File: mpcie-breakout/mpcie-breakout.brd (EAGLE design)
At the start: 50 x 70 mm, 34 parts, among them K1 694108106102, U1 IP4234CZ6, U2 LD1085D2T33R, X1 MPCIE-JAE, X2 MINI-USB-SHIELD-UX60-MB-5ST

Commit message: mpci-breakout: Add BOM attributes + export BOM
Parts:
- R1, R2, R3: value (none) -> 47

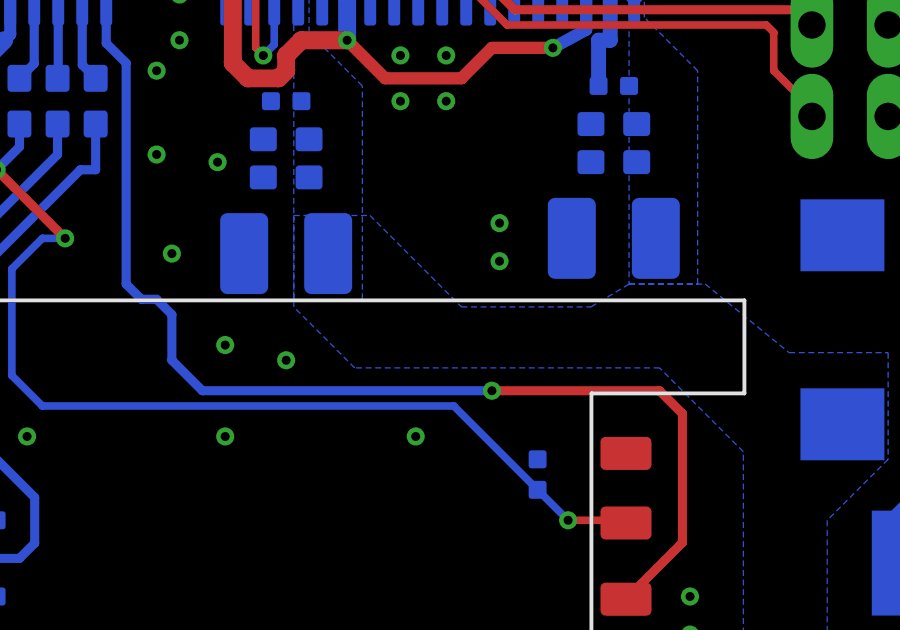
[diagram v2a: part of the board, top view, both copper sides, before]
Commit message: mpcie-breakout: change 100uF caps from 1210 to 1206, reducing height
The current 100uF caps are too high at 2.9mm.  They touch the shielding
can of Quectel EC-20 modules, for exampel.  Let's use 1206 packaged
versions at 1.6mm instead.  Also, add two more, for safety.
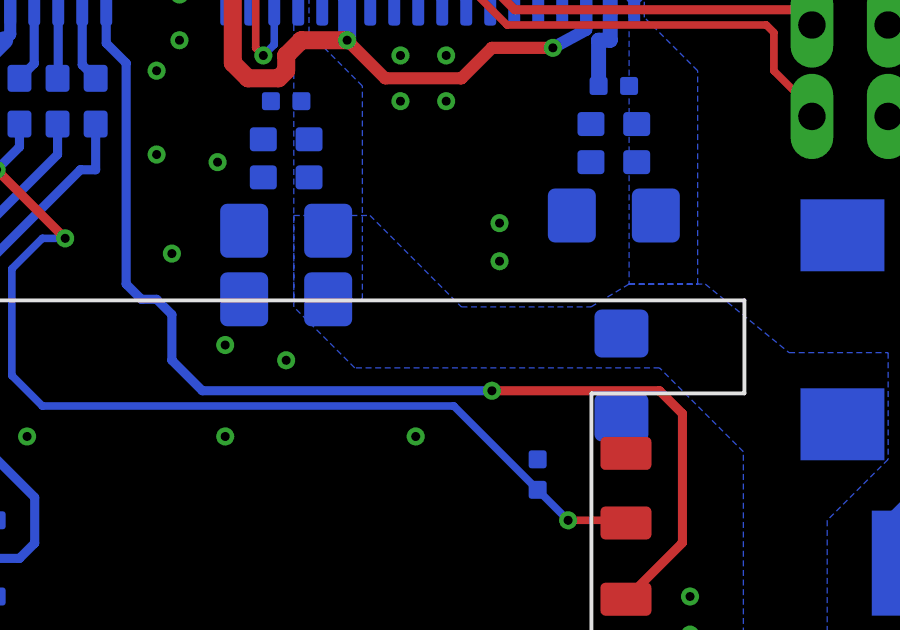
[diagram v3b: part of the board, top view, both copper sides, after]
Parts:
- added C10, C11: 100u, rc-sysmocom:1206
- C105, C109: device rc-sysmocom:C1210 -> rc-sysmocom:1206
- moved C105 0.76 mm to (16.5, 42.7)
- moved C109 0.76 mm to (27.4, 43.2)
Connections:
- net GND: now also C10.1, C11.1
- net VCC_3V3: now also C10.2, C11.2

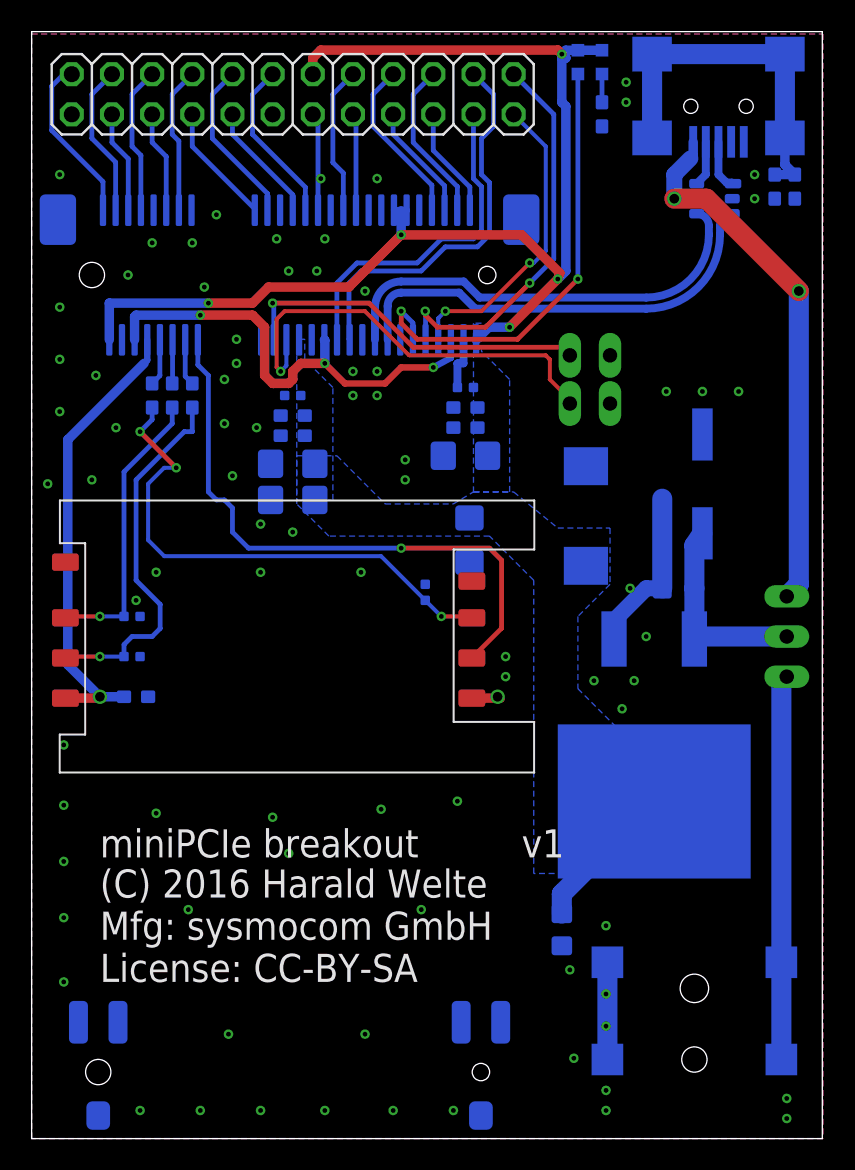
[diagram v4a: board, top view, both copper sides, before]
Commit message: mpcie-breakout: Add series LED for LED_WWAN
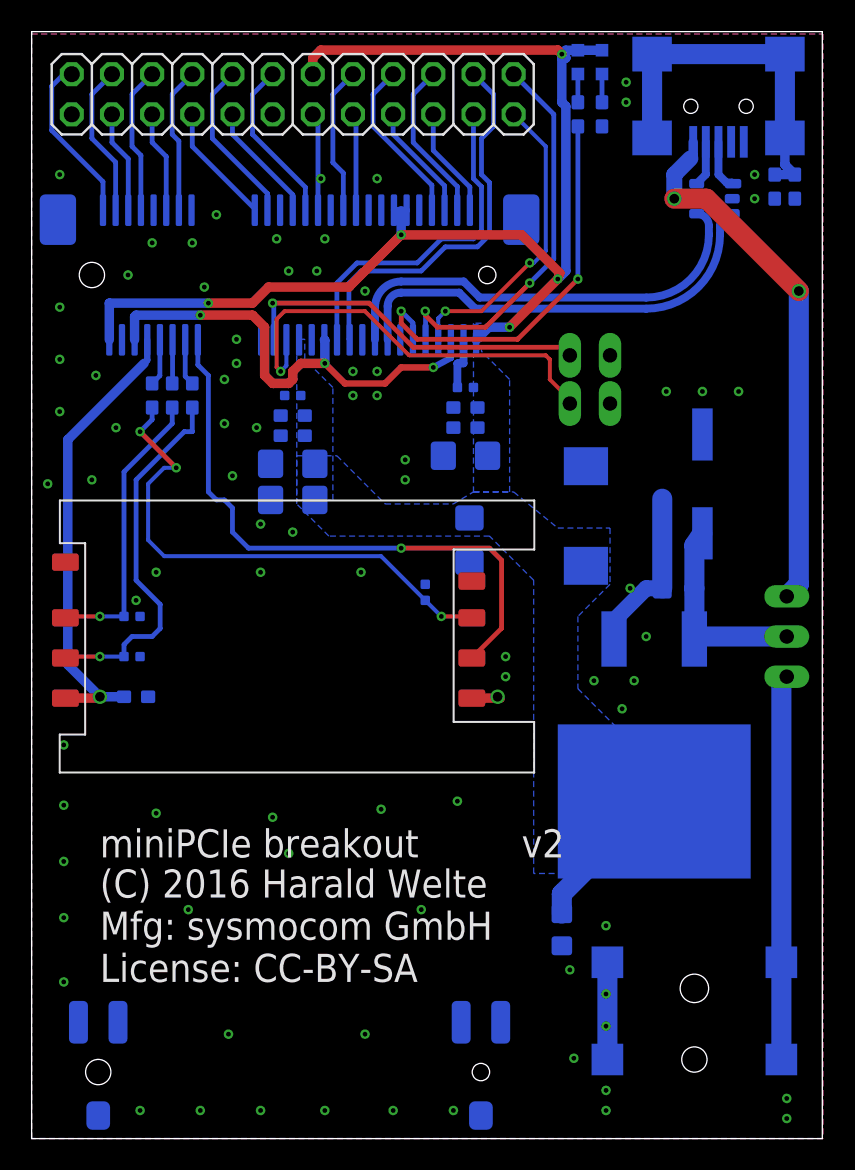
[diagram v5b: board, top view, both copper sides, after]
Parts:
- added R6: 330, rc-sysmocom:_0603
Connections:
- new net N$2: LED1.C, R6.1
- net N$3: now also R6.2; no longer LED1.C
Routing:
- net N$3: track 29.0 -> 25.7 mm
- net N$2: track 0.00 -> 1.79 mm
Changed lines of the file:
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@@
 </plain>
 <attributes>
-<attribute name="VERSION" value="v1"/>
+<attribute name="VERSION" value="v2"/>
 </attributes>
 <variantdefs>
@@
 <attribute name="VALUE" x="25.781" y="36.2585" size="0.508" layer="28" font="vector" ratio="10" rot="MR90"/>
 </element>
+<element name="R6" library="rc-sysmocom" package="_0603" value="330" x="34.544" y="64.77" rot="MR270">
+<attribute name="LINK" value="http://www.digikey.com/product-detail/en/yageo/RC0603JR-07330RL/311-330GRCT-ND/729716" x="34.544" y="64.77" size="1.778" layer="28" rot="MR270" display="off"/>
+<attribute name="MANUFACTURERPARTNUMBER" value="RC0603JR-07330RL" x="34.544" y="64.77" size="1.778" layer="28" rot="MR270" display="off"/>
+<attribute name="ROHSCERTIFICATE" value="UNKNOWN ROHS CERTIFICATE" x="34.544" y="64.77" size="1.778" layer="28" rot="MR270" display="off"/>
+<attribute name="SOURCE" value="DIGIKEY" x="34.544" y="64.77" size="1.778" layer="28" rot="MR270" display="off"/>
+<attribute name="CLASS" value="RESISTOR" x="34.544" y="64.77" size="1.778" layer="28" rot="MR270" display="off"/>
+<attribute name="POPULATED" value="TRUE" x="34.544" y="64.77" size="1.778" layer="28" rot="MR270" display="off"/>
+<attribute name="MANUFACTURER" value="Yageo" x="34.544" y="64.77" size="1.778" layer="28" rot="MR270" display="off"/>
+<attribute name="SOURCEPARTNUMBER" value="311-330GRCT-ND" x="34.544" y="64.77" size="1.778" layer="28" rot="MR270" display="off"/>
+<attribute name="DESCRIPTION" value="RES SMD 330 OHM 5% 1/10W 0603" x="34.544" y="64.77" size="1.778" layer="28" rot="MR270" display="off"/>
+</element>
 </elements>
 <signals>
@@
 <signal name="N$3">
 <contactref element="X1" pad="42"/>
-<contactref element="LED1" pad="C"/>
 <wire x1="24.111875" y1="50.51" x2="24.111875" y2="51.580125" width="0.3048" layer="16"/>
 <wire x1="24.111875" y1="51.580125" x2="23.368" y2="52.324" width="0.3048" layer="16"/>
@@
 <wire x1="30.734" y1="50.546" x2="34.544" y2="54.356" width="0.3048" layer="1"/>
 <via x="34.544" y="54.356" extent="1-16" drill="0.3"/>
-<wire x1="34.544" y1="54.356" x2="34.544" y2="67.322" width="0.3048" layer="16"/>
+<contactref element="R6" pad="2"/>
+<wire x1="34.544" y1="54.356" x2="34.544" y2="64.008" width="0.3048" layer="16"/>
 </signal>
 <signal name="N$4">
@@
 <wire x1="36.068" y1="67.322" x2="36.068" y2="65.532" width="0.3048" layer="16"/>
 </signal>
+<signal name="N$2">
+<contactref element="LED1" pad="C"/>
+<contactref element="R6" pad="1"/>
+<wire x1="34.544" y1="67.322" x2="34.544" y2="65.532" width="0.3048" layer="16"/>
+</signal>
 </signals>

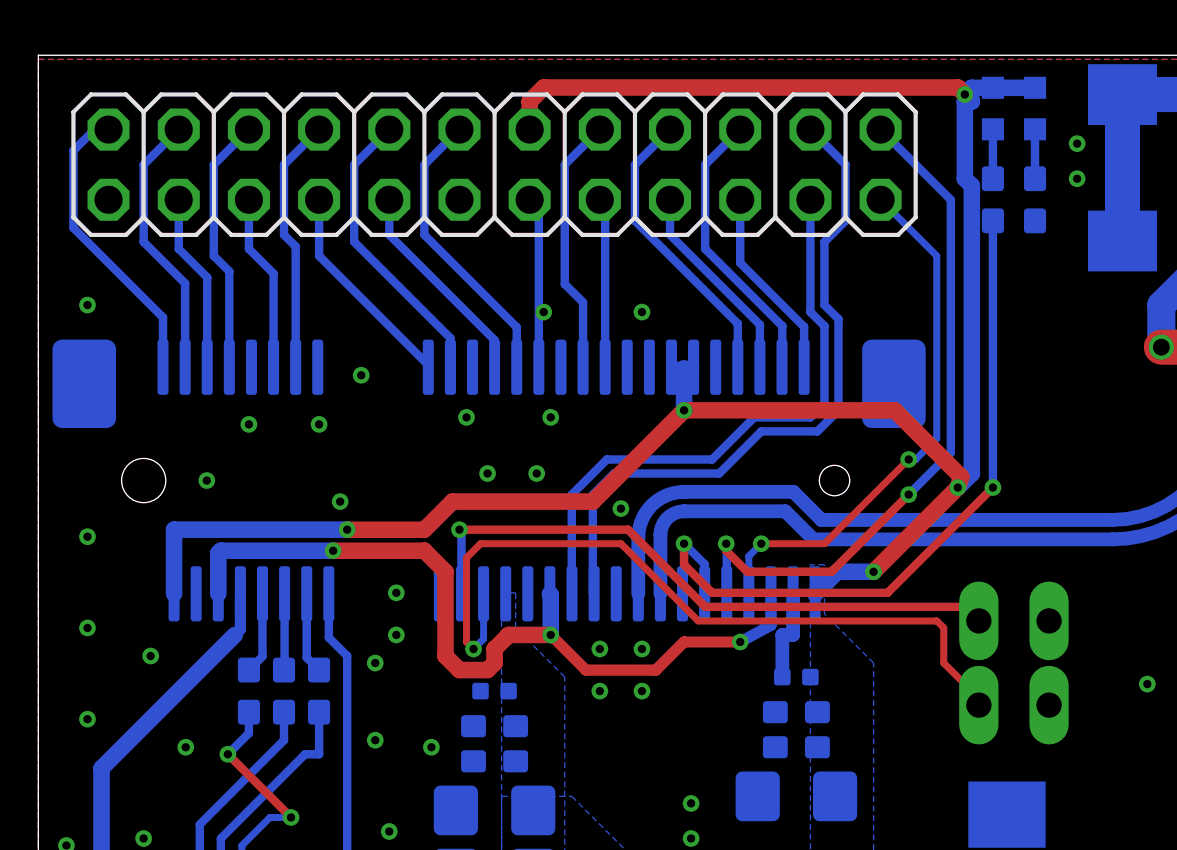
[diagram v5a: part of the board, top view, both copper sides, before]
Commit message: mpcie-breakout: fix DRC violations (clearance)
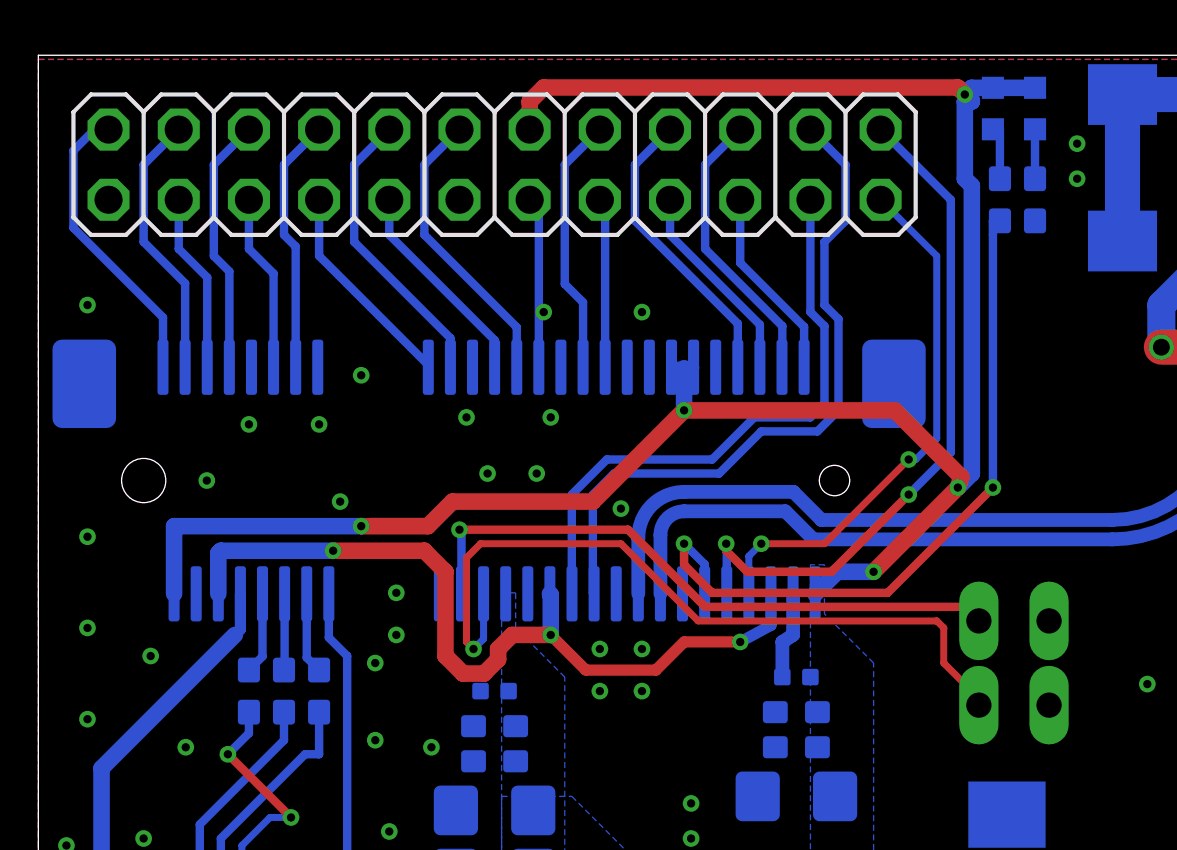
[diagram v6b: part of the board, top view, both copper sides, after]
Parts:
- moved R6 0.25 mm to (34.8, 64.8)
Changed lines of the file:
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@@
 <attribute name="VALUE" x="25.781" y="36.2585" size="0.508" layer="28" font="vector" ratio="10" rot="MR90"/>
 </element>
-<element name="R6" library="rc-sysmocom" package="_0603" value="330" x="34.544" y="64.77" rot="MR270">
-<attribute name="LINK" value="http://www.digikey.com/product-detail/en/yageo/RC0603JR-07330RL/311-330GRCT-ND/729716" x="34.544" y="64.77" size="1.778" layer="28" rot="MR270" display="off"/>
-<attribute name="MANUFACTURERPARTNUMBER" value="RC0603JR-07330RL" x="34.544" y="64.77" size="1.778" layer="28" rot="MR270" display="off"/>
-<attribute name="ROHSCERTIFICATE" value="UNKNOWN ROHS CERTIFICATE" x="34.544" y="64.77" size="1.778" layer="28" rot="MR270" display="off"/>
-<attribute name="SOURCE" value="DIGIKEY" x="34.544" y="64.77" size="1.778" layer="28" rot="MR270" display="off"/>
-<attribute name="CLASS" value="RESISTOR" x="34.544" y="64.77" size="1.778" layer="28" rot="MR270" display="off"/>
-<attribute name="POPULATED" value="TRUE" x="34.544" y="64.77" size="1.778" layer="28" rot="MR270" display="off"/>
-<attribute name="MANUFACTURER" value="Yageo" x="34.544" y="64.77" size="1.778" layer="28" rot="MR270" display="off"/>
-<attribute name="SOURCEPARTNUMBER" value="311-330GRCT-ND" x="34.544" y="64.77" size="1.778" layer="28" rot="MR270" display="off"/>
-<attribute name="DESCRIPTION" value="RES SMD 330 OHM 5% 1/10W 0603" x="34.544" y="64.77" size="1.778" layer="28" rot="MR270" display="off"/>
+<element name="R6" library="rc-sysmocom" package="_0603" value="330" x="34.798" y="64.77" rot="MR270">
+<attribute name="LINK" value="http://www.digikey.com/product-detail/en/yageo/RC0603JR-07330RL/311-330GRCT-ND/729716" x="34.798" y="64.77" size="1.778" layer="28" rot="MR270" display="off"/>
+<attribute name="MANUFACTURERPARTNUMBER" value="RC0603JR-07330RL" x="34.798" y="64.77" size="1.778" layer="28" rot="MR270" display="off"/>
+<attribute name="ROHSCERTIFICATE" value="UNKNOWN ROHS CERTIFICATE" x="34.798" y="64.77" size="1.778" layer="28" rot="MR270" display="off"/>
+<attribute name="SOURCE" value="DIGIKEY" x="34.798" y="64.77" size="1.778" layer="28" rot="MR270" display="off"/>
+<attribute name="CLASS" value="RESISTOR" x="34.798" y="64.77" size="1.778" layer="28" rot="MR270" display="off"/>
+<attribute name="POPULATED" value="TRUE" x="34.798" y="64.77" size="1.778" layer="28" rot="MR270" display="off"/>
+<attribute name="MANUFACTURER" value="Yageo" x="34.798" y="64.77" size="1.778" layer="28" rot="MR270" display="off"/>
+<attribute name="SOURCEPARTNUMBER" value="311-330GRCT-ND" x="34.798" y="64.77" size="1.778" layer="28" rot="MR270" display="off"/>
+<attribute name="DESCRIPTION" value="RES SMD 330 OHM 5% 1/10W 0603" x="34.798" y="64.77" size="1.778" layer="28" rot="MR270" display="off"/>
 </element>
 </elements>
@@
 <via x="6.604" y="34.036" extent="1-16" drill="0.3"/>
 <wire x1="27.311875" y1="50.51" x2="27.311875" y2="49.022" width="0.5" layer="16"/>
-<wire x1="27.311875" y1="49.022" x2="26.924" y2="49.022" width="0.5" layer="16"/>
-<wire x1="26.924" y1="49.022" x2="26.924" y2="47.498" width="0.5" layer="16"/>
+<wire x1="27.311875" y1="49.022" x2="26.924" y2="48.768" width="0.5" layer="16"/>
+<wire x1="26.924" y1="48.768" x2="26.924" y2="47.498" width="0.5" layer="16"/>
 <via x="29.972" y="30.48" extent="1-16" drill="0.3"/>
 <via x="29.972" y="29.21" extent="1-16" drill="0.3"/>
@@
 <wire x1="13.97" y1="52.07" x2="14.732" y2="51.308" width="0.6" layer="1"/>
 <wire x1="14.732" y1="51.308" x2="14.732" y2="48.26" width="0.6" layer="1"/>
-<wire x1="14.732" y1="48.26" x2="15.24" y2="47.752" width="0.6" layer="1"/>
-<wire x1="15.24" y1="47.752" x2="16.256" y2="47.752" width="0.6" layer="1"/>
-<wire x1="16.256" y1="47.752" x2="16.51" y2="48.006" width="0.6" layer="1"/>
-<wire x1="16.51" y1="48.006" x2="16.51" y2="48.514" width="0.6" layer="1"/>
-<wire x1="16.51" y1="48.514" x2="17.018" y2="49.022" width="0.6" layer="1"/>
-<wire x1="17.018" y1="49.022" x2="18.542" y2="49.022" width="0.6" layer="1"/>
+<wire x1="14.732" y1="48.26" x2="15.3675" y2="47.6245" width="0.6" layer="1"/>
+<wire x1="15.3675" y1="47.6245" x2="16.1285" y2="47.6245" width="0.6" layer="1"/>
+<wire x1="16.1285" y1="47.6245" x2="16.6375" y2="48.1335" width="0.6" layer="1"/>
+<wire x1="16.6375" y1="48.1335" x2="16.6375" y2="48.514" width="0.6" layer="1"/>
+<wire x1="16.6375" y1="48.514" x2="17.1455" y2="49.022" width="0.6" layer="1"/>
+<wire x1="17.1455" y1="49.022" x2="18.542" y2="49.022" width="0.6" layer="1"/>
 <via x="18.542" y="49.022" extent="1-16" drill="0.3"/>
 <wire x1="18.542" y1="49.022" x2="18.542" y2="50.479875" width="0.6" layer="16"/>
@@
 <wire x1="33.528" y1="65.532" x2="33.782" y2="65.278" width="0.6" layer="16"/>
 <wire x1="33.782" y1="65.278" x2="33.782" y2="54.864" width="0.6" layer="16"/>
-<wire x1="4.911875" y1="50.51" x2="4.911875" y2="52.832" width="0.6" layer="16"/>
-<wire x1="4.911875" y1="52.832" x2="11.176" y2="52.832" width="0.6" layer="16"/>
+<wire x1="4.911875" y1="50.51" x2="4.911875" y2="52.9585" width="0.6" layer="16"/>
+<wire x1="4.911875" y1="52.9585" x2="11.684" y2="52.9585" width="0.6" layer="16"/>
 <wire x1="23.711875" y1="58.71" x2="22.911875" y2="58.71" width="0.4064" layer="16"/>
 <wire x1="23.711875" y1="58.71" x2="23.711875" y2="58.674" width="0.4064" layer="16"/>
@@
 <wire x1="30.988" y1="57.15" x2="33.401" y2="54.737" width="0.6" layer="1"/>
 <wire x1="33.401" y1="54.737" x2="33.274" y2="54.356" width="0.6" layer="1"/>
-<via x="11.176" y="52.832" extent="1-16" drill="0.3"/>
-<wire x1="11.176" y1="52.832" x2="13.97" y2="52.832" width="0.6" layer="1"/>
-<wire x1="13.97" y1="52.832" x2="14.986" y2="53.848" width="0.6" layer="1"/>
+<via x="11.684" y="52.9585" extent="1-16" drill="0.3"/>
+<wire x1="11.684" y1="52.9585" x2="14.0975" y2="52.9595" width="0.6" layer="1"/>
+<wire x1="14.0975" y1="52.9595" x2="14.986" y2="53.848" width="0.6" layer="1"/>
 <wire x1="14.986" y1="53.848" x2="20.066" y2="53.848" width="0.6" layer="1"/>
 <wire x1="20.066" y1="53.848" x2="23.368" y2="57.15" width="0.6" layer="1"/>
@@
 <via x="34.544" y="54.356" extent="1-16" drill="0.3"/>
 <contactref element="R6" pad="2"/>
-<wire x1="34.544" y1="54.356" x2="34.544" y2="64.008" width="0.3048" layer="16"/>
+<wire x1="34.544" y1="54.356" x2="34.544" y2="63.5" width="0.3048" layer="16"/>
+<wire x1="34.544" y1="63.5" x2="34.544" y2="64.008" width="0.3048" layer="16"/>
+<wire x1="34.544" y1="64.008" x2="34.798" y2="64.008" width="0.3048" layer="16"/>
 </signal>
 <signal name="N$4">
@@
 <contactref element="LED1" pad="C"/>
 <contactref element="R6" pad="1"/>
-<wire x1="34.544" y1="67.322" x2="34.544" y2="65.532" width="0.3048" layer="16"/>
+<wire x1="34.544" y1="67.322" x2="34.798" y2="67.322" width="0.3048" layer="16"/>
+<wire x1="34.798" y1="67.322" x2="34.798" y2="65.532" width="0.3048" layer="16"/>
 </signal>
 </signals>
